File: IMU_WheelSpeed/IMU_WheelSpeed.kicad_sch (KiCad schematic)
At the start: 10 parts, among them J1 Conn_01x06_Socket, U1 PeripheralSOM, U2 LSM6DSL, U4 TPS71518__SC70

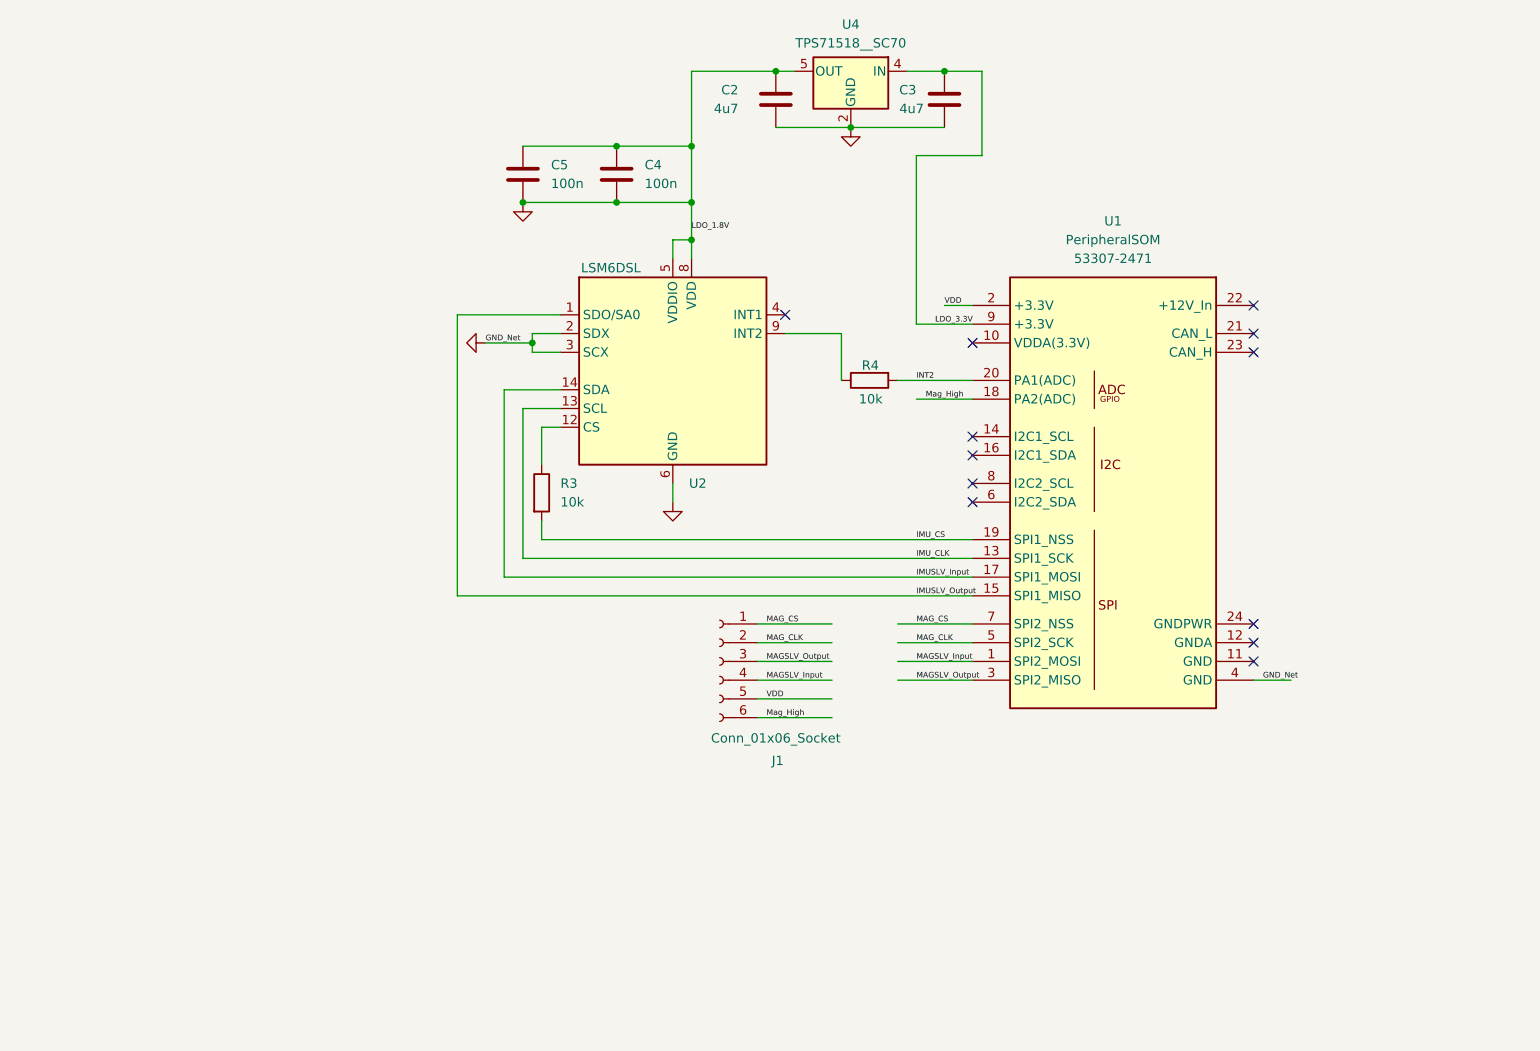
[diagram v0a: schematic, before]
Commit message: added to schematic
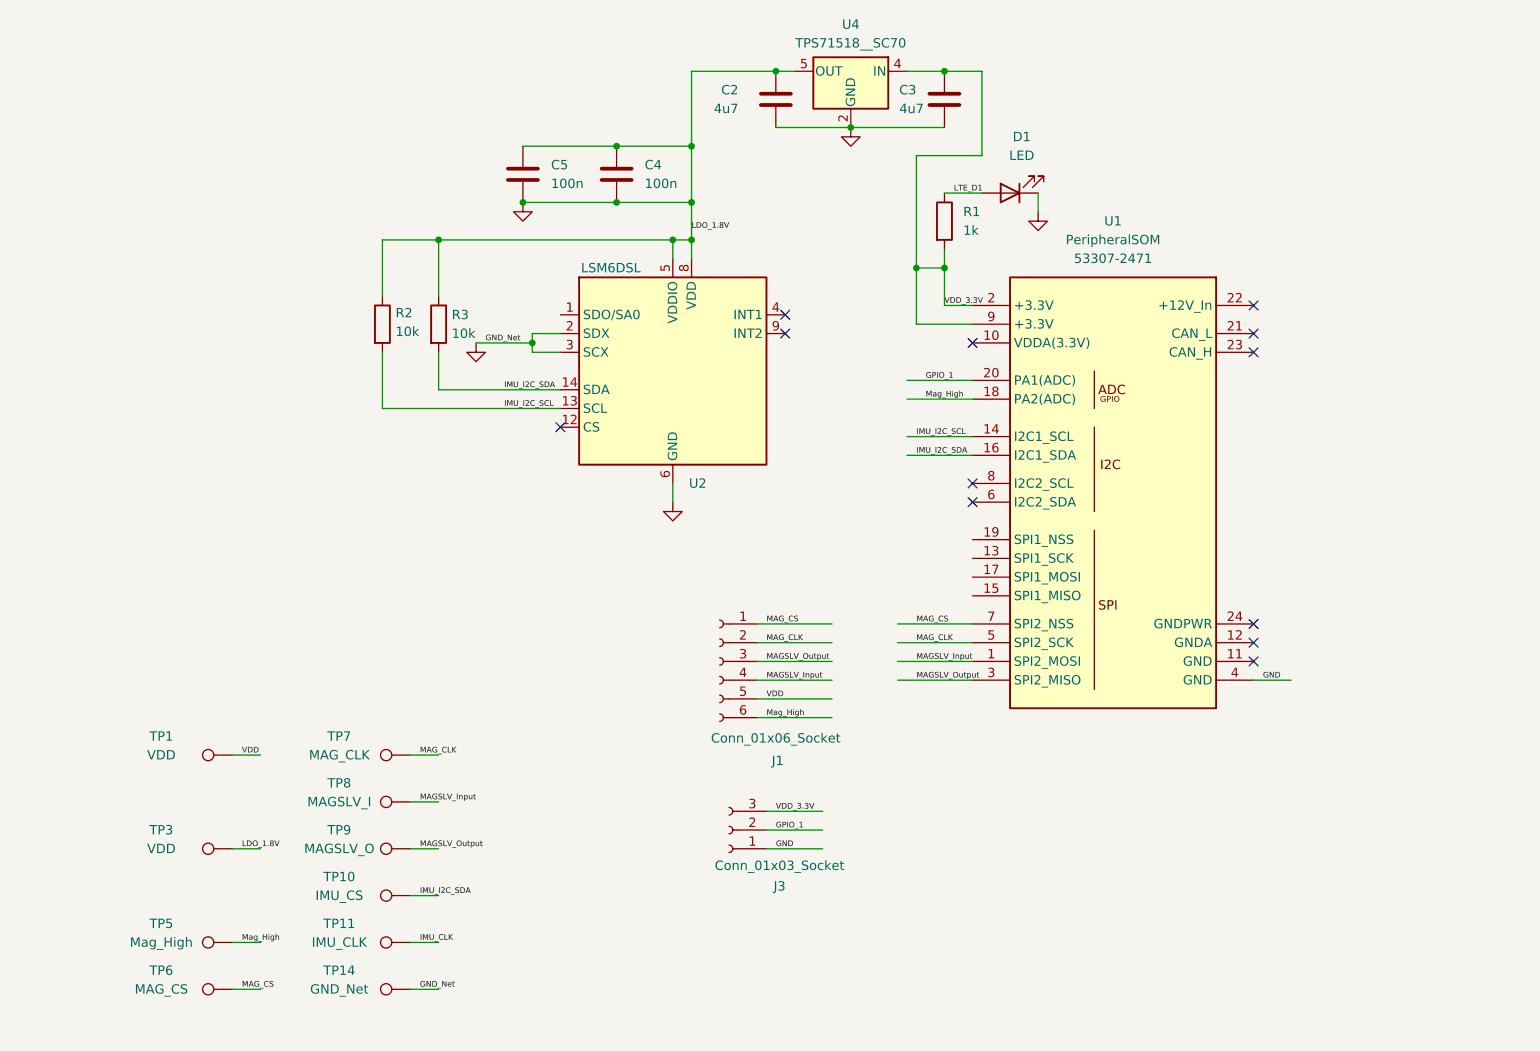
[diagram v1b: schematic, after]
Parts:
- removed R4: 10k, Resistor_SMD:R_0805_2012Metric, symbol Device:R
- added D1: LED, LED_SMD:LED_0805_2012Metric, symbol Device:LED
- added J3: Conn_01x03_Socket, Connector_Molex:Molex_Nano-Fit_105313-xx03_1x03_P2.50mm_Horizontal, symbol Connector:Conn_01x03_Socket
- added R1: 1k, Resistor_SMD:R_0805_2012Metric, symbol Device:R
- added R2: 10k, Resistor_SMD:R_0805_2012Metric, symbol Device:R
- added TP1, TP3: VDD, TestPoint:TestPoint_THTPad_D3.0mm_Drill1.5mm, symbol Connector:TestPoint
- added TP10: IMU_CS, TestPoint:TestPoint_THTPad_D3.0mm_Drill1.5mm, symbol Connector:TestPoint
- added TP11: IMU_CLK, TestPoint:TestPoint_THTPad_D3.0mm_Drill1.5mm, symbol Connector:TestPoint
- added TP14: GND_Net, TestPoint:TestPoint_THTPad_D3.0mm_Drill1.5mm, symbol Connector:TestPoint
- added TP5: Mag_High, TestPoint:TestPoint_THTPad_D3.0mm_Drill1.5mm, symbol Connector:TestPoint
- added TP6: MAG_CS, TestPoint:TestPoint_THTPad_D3.0mm_Drill1.5mm, symbol Connector:TestPoint
- added TP7: MAG_CLK, TestPoint:TestPoint_THTPad_D3.0mm_Drill1.5mm, symbol Connector:TestPoint
- added TP8: MAGSLV_I, TestPoint:TestPoint_THTPad_D3.0mm_Drill1.5mm, symbol Connector:TestPoint
- added TP9: MAGSLV_O, TestPoint:TestPoint_THTPad_D3.0mm_Drill1.5mm, symbol Connector:TestPoint
- J1: footprint Connector_FFC-FPC:Molex_200528-0060_1x06-1MP_P1.00mm_Horizontal -> Connector_Molex:Molex_Nano-Fit_105313-xx06_1x06_P2.50mm_Horizontal
- U4: footprint Package_TO_SOT_SMD:SOT-353_SC-70-5 -> UTSVT_Power:LDO_3.3_to_1.8_2.2mmx1.3mm
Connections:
- net GND: now also D1.1 (K), J3.1 (Pin_1), TP14.1
- net IMU_CLK: now also TP11.1; no longer U1.13 (SPI1_SCK), U2.13 (SCL)
- net LDO_1.8V: now also R3.1, R2.1, TP3.1
- net MAGSLV_Input: now also TP8.1
- net MAGSLV_Output: now also TP9.1
- net MAG_CLK: now also TP7.1
- net MAG_CS: now also TP6.1
- net Mag_High: now also TP5.1
- net VDD: now also TP1.1; no longer U1.2 (+3.3V)
- net at U2.12 (CS): no longer R3.1
- net IMU_I2C_SCL: now reaches U1.14 (I2C1_SCL)
- net IMU_I2C_SCL: now also U2.13 (SCL), R2.2
- net IMU_I2C_SDA: now reaches U1.16 (I2C1_SDA)
- net IMU_I2C_SDA: now also R3.2, U2.14 (SDA), TP10.1
- net IMUSLV_Input: no longer names the net of U1.17 (SPI1_MOSI)
- net IMUSLV_Input: no longer U2.14 (SDA)
- net IMUSLV_Output: no longer names the net of U2.1 (SDO/SA0)
- net IMUSLV_Output: no longer U1.15 (SPI1_MISO)
- net IMU_CS: no longer names the net of U1.19 (SPI1_NSS)
- net IMU_CS: no longer R3.2
- net INT2 renamed GPIO_1
- net GPIO_1: now also J3.2 (Pin_2)
- net LDO_3.3V renamed VDD_3.3V
- net VDD_3.3V: now also U1.2 (+3.3V), J3.3 (Pin_3), R1.2
- new net LTE_D1: D1.2 (A), R1.1

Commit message: redid layout
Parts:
- TP10: value IMU_CS -> IMU_I2C_SDA
- TP14: value GND_Net -> GND
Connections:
- net VDD: no longer J1.5 (Pin_5)
- net VDD_3.3V: now also J1.5 (Pin_5)
- net IMU_CLK renamed IMU_I2C_SLC
- no-connect marks 12 -> 17
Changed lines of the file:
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@@
+	)
+	(no_connect
+		(at 124.46 64.77)
+	)
+	(no_connect
+		(at 180.34 100.33)
 	)
 	(no_connect
@@
 	)
 	(no_connect
+		(at 180.34 97.79)
+	)
+	(no_connect
+		(at 180.34 95.25)
+	)
+	(no_connect
+		(at 180.34 102.87)
+	)
+	(no_connect
 		(at 218.44 111.76)
 	)
@@
 		)
 	)
-	(label "VDD"
+	(label "VDD_3.3V"
 		(at 152.4 116.84 0)
 		(fields_autoplaced yes)
@@
 		)
 	)
-	(label "IMU_CLK"
+	(label "IMU_I2C_SLC"
 		(at 105.41 149.86 0)
 		(fields_autoplaced yes)
@@
 		)
 	)
-	(label "GND_Net"
+	(label "GND"
 		(at 105.41 156.21 0)
 		(fields_autoplaced yes)
@@
 		)
 	)
-	(label "LDO_1.8V"
-		(at 142.24 53.34 0)
-		(fields_autoplaced yes)
-		(effects
-			(font
-				(size 0.762 0.762)
-			)
-			(justify left bottom)
-		)
-	)
 	(label "GND_Net"
 		(at 114.3 68.58 0)
@@
 		)
 	)
+	(label "LDO_1.8V"
+		(at 143.51 31.75 0)
+		(fields_autoplaced yes)
+		(effects
+			(font
+				(size 0.762 0.762)
+			)
+			(justify left bottom)
+		)
+	)
 	(label "MAGSLV_Input"
 		(at 105.41 130.81 0)
@@
 	)
 	(label "LDO_1.8V"
-		(at 81.28 137.16 0)
+		(at 80.01 137.16 0)
 		(fields_autoplaced yes)
 		(effects
@@
 			)
 		)
-		(property "Value" "GND_Net"
+		(property "Value" "GND"
 			(at 94.488 156.21 90)
 			(effects
@@
 			)
 		)
-		(property "Value" "IMU_CS"
-			(at 94.488 143.51 90)
-			(effects
-				(font
+		(property "Value" "IMU_I2C_SDA"
+			(at 92.964 143.51 90)
+			(effects
+				(font

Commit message: Check up
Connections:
- net IMU_I2C_SLC is gone; now on net IMU_I2C_SCL: TP11.1
- net VDD is gone; now on net VDD_3.3V: TP1.1
- net GND: now also C2.2, C3.2, C4.2, C5.2, R2.1, R3.1, U2.5 (VDDIO), U2.8 (VDD), U4.2 (GND)
- net LDO_1.8V: no longer C4.2, C5.2, R2.1, R3.1, U2.5 (VDDIO), U2.8 (VDD)
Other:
- note added: "3.3V to 1.8V LDO"
- note added: "Hall-Effect Connector"
- note added: "IMU Module with Bypass Caps"
- note added: "Peripheral SOM Connector"
- note added: "Potentiometer Connector"
- note added: "TestPoints"
- company: (none) -> LHR Solar
- title: (none) -> Wheel Speed and IMU Board
- moved on the sheet: C2, C3, C4, C5, D1, J1, J3, R1, R2, R3, TP1, TP10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

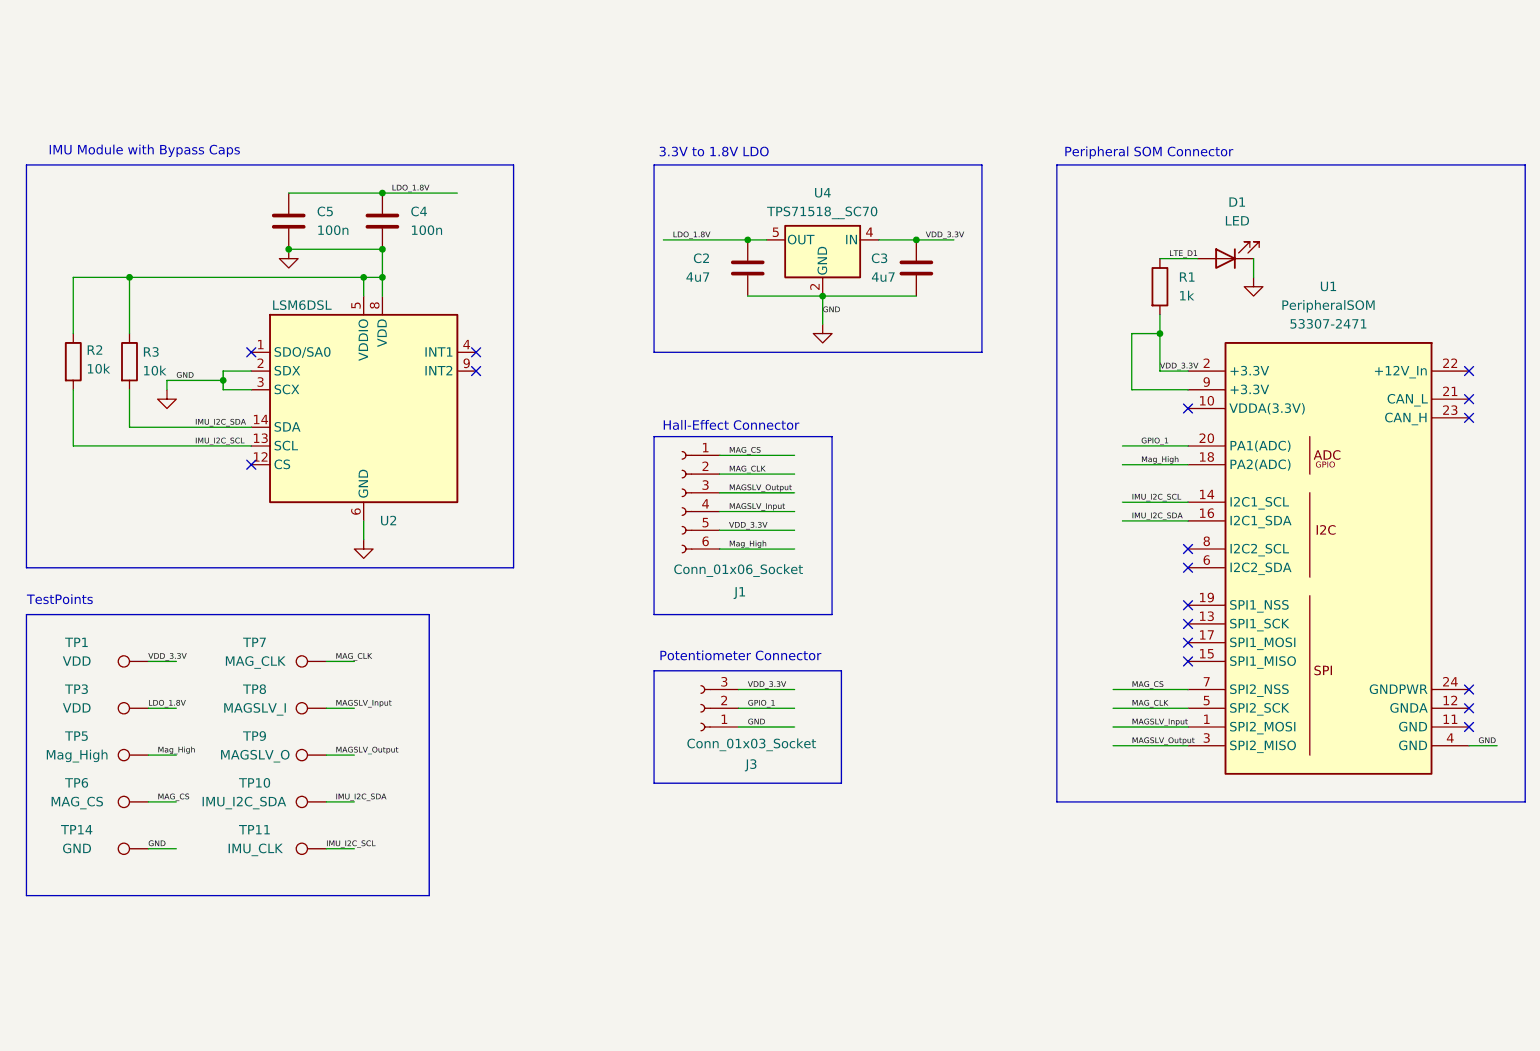
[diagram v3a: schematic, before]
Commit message: (label "LDO_1.8V" (at 124.46 142.24 0) (fields_auteplaced yes)   (effects (font (size 0.762 0.762)) (justify left bottom)) (uuid "5df45f02-f0ff-424b-b1b0-8f9540b4e896") ) (label "LDO_1.8V" (at 124.46 142.24 0) (fields_autoplaced yes)   (effects (font (size 0.762 0.762)) (justify left bottom)) (uuid "5df45f02-f0ff-424b-b1b0-8f9540b4e896") )
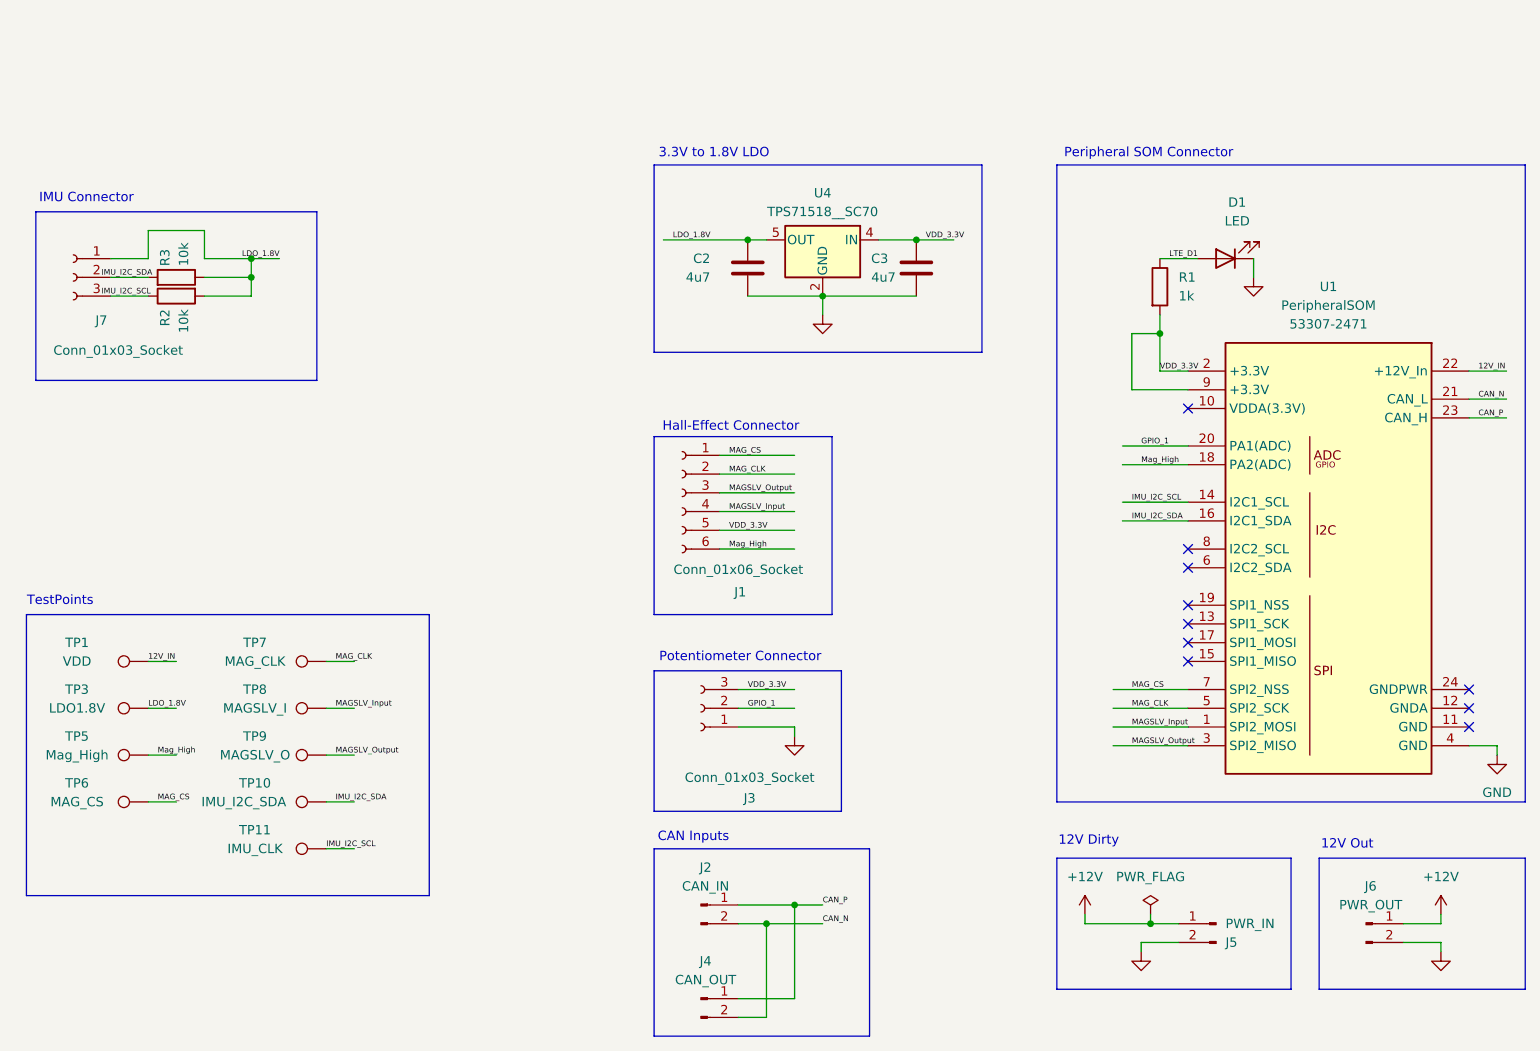
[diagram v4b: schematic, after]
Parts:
- removed C4, C5: 100n, Capacitor_SMD:C_0805_2012Metric, symbol Device:C
- removed TP14: GND, TestPoint:TestPoint_THTPad_D3.0mm_Drill1.5mm, symbol Connector:TestPoint
- removed U2: LSM6DSL, Package_LGA:LGA-14_3x2.5mm_P0.5mm_LayoutBorder3x4y, symbol Sensor_Motion:LSM6DSL
- added J2: CAN_IN, UTSVT_Connectors:CONN_SD-43650-006_02_MOL, symbol Connector:Conn_01x02_Pin
- added J4: CAN_OUT, UTSVT_Connectors:CONN_SD-43650-006_02_MOL, symbol Connector:Conn_01x02_Pin
- added J5: PWR_IN, UTSVT_Connectors:CONN_SD-43650-006_02_MOL, symbol Connector:Conn_01x02_Pin
- added J6: PWR_OUT, UTSVT_Connectors:CONN_SD-43650-006_02_MOL, symbol Connector:Conn_01x02_Pin
- added J7: Conn_01x03_Socket, Connector_Molex:Molex_Nano-Fit_105313-xx03_1x03_P2.50mm_Horizontal, symbol Connector:Conn_01x03_Socket
- TP3: value VDD -> LDO1.8V
- U4: Mouser Link (none) -> https://www.mouser.com/ProductDetail/Texas-Instruments/TPS7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
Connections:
- net GND: now also J5.2 (Pin_2), J6.2 (Pin_2); no longer R2.1, R3.1
- net IMU_I2C_SCL: no longer R2.2
- net IMU_I2C_SDA: no longer R3.2
- net LDO_1.8V: now also R2.2, R3.1, J7.1 (Pin_1)
- net VDD_3.3V: no longer TP1.1
- net CAN_N: now reaches U1.21 (CAN_L)
- net CAN_N: now also J2.2 (Pin_2), J4.2 (Pin_2)
- net 12V_IN: now reaches U1.22 (+12V_In)
- net 12V_IN: now also TP1.1
- net CAN_P: now reaches U1.23 (CAN_H)
- net CAN_P: now also J2.1 (Pin_1), J4.1 (Pin_1)
- new net: J7.2 (Pin_2), R3.2
- new net: J7.3 (Pin_3), R2.1
- new net +12V: J5.1 (Pin_1), J6.1 (Pin_1)
- no-connect marks 17 -> 10
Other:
- note added: "12V Dirty"
- note added: "12V Out"
- note added: "CAN Inputs"
- note added: "IMU Connector"
- note removed: "IMU Module with Bypass Caps"

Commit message: Switched connectors
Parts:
- J1: footprint Connector_Molex:Molex_Nano-Fit_105313-xx06_1x06_P2.50mm_Horizontal -> UTSVT_Connectors:Molex_MicroFit_01x06_Horizontal
- J3, J7: footprint Connector_Molex:Molex_Nano-Fit_105313-xx03_1x03_P2.50mm_Horizontal -> UTSVT_Connectors:Molex_MicroFit3.0_1x3xP3.00mm_PolarizingPeg_Vertical
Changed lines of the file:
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@@
 			)
 		)
-		(property "Footprint" "Connector_Molex:Molex_Nano-Fit_105313-xx03_1x03_P2.50mm_Horizontal"
+		(property "Footprint" "UTSVT_Connectors:Molex_MicroFit3.0_1x3xP3.00mm_PolarizingPeg_Vertical"
 			(at 143.51 118.11 0)
 			(effects
@@
 			)
 		)
-		(property "Footprint" "Connector_Molex:Molex_Nano-Fit_105313-xx03_1x03_P2.50mm_Horizontal"
+		(property "Footprint" "UTSVT_Connectors:Molex_MicroFit3.0_1x3xP3.00mm_PolarizingPeg_Vertical"
 			(at 58.42 59.69 0)
 			(effects
@@
 			)
 		)
-		(property "Footprint" "Connector_Molex:Molex_Nano-Fit_105313-xx06_1x06_P2.50mm_Horizontal"
+		(property "Footprint" "UTSVT_Connectors:Molex_MicroFit_01x06_Horizontal"
 			(at 140.97 88.9 0)
 			(effects
